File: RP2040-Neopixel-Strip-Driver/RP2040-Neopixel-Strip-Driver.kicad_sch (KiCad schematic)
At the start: 0 parts

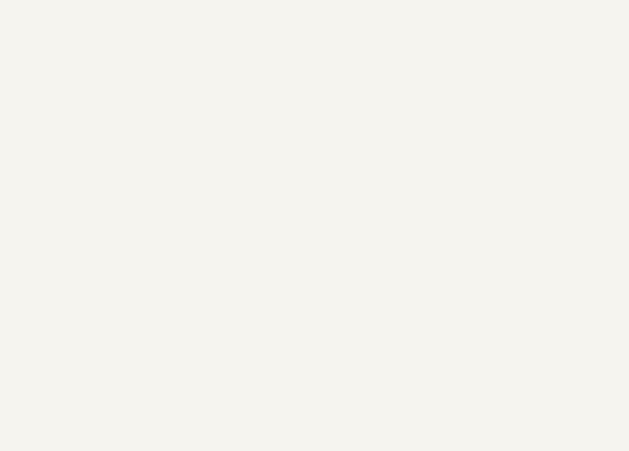
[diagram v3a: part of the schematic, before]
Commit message: Added level shifter
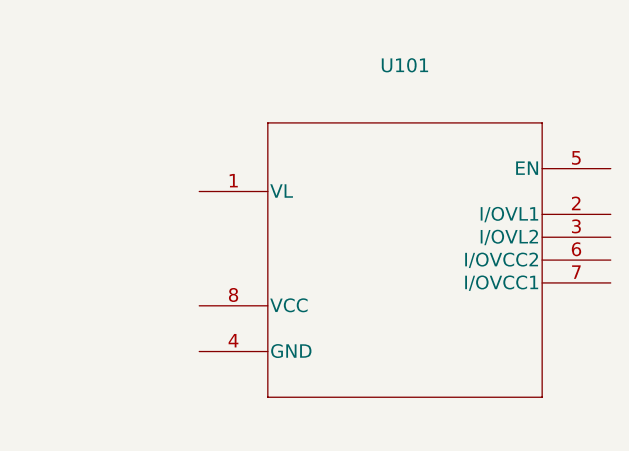
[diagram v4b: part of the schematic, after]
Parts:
- added U101: (no value), symbol NLSX4302EBMUTCG:NLSX4302EBMUTCG
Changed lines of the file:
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@@
     (comment 4 "https://github.com/mrangen/RP2040-Dev-Board")
+  )
+  (symbol (lib_id "NLSX4302EBMUTCG:NLSX4302EBMUTCG") (at 168.91 67.31 0) (unit 1)
+    (in_bom yes) (on_board yes) (fields_autoplaced)
+    (property "Reference" "U101" (id 0) (at 191.77 53.34 0)
+      (effects (font (size 1.524 1.524)))
+    )
+    (property "Value" "" (id 1) (at 191.77 57.15 0)
+      (effects (font (size 1.524 1.524)))
+    )
+    (property "Footprint" "" (id 2) (at 191.77 58.674 0)
+      (effects (font (size 1.524 1.524)) hide)
+    )
+    (property "Datasheet" "" (id 3) (at 168.91 67.31 0)
+      (effects (font (size 1.524 1.524)))
+    )
+    (property "JLCPCB P/N" "C893527" (id 4) (at 168.91 67.31 0)
+      (effects (font (size 1.27 1.27)) hide)
+    )
+    (pin "1")
+    (pin "2")
+    (pin "3")
+    (pin "4")
+    (pin "5")
+    (pin "6")
+    (pin "7")
+    (pin "8")
   )
   (sheet (at 82.55 50.8) (size 45.72 40.64) (fields_autoplaced)
@@
       (reference "SW202") (unit 1) (value "~{USB_BOOT}") (footprint "Breadstick Footprints:GT-TC029B-H025-L1N")
     )
+    (path "/61abfe14-530f-45cb-bac5-bff48de16e05"
+      (reference "U101") (unit 1) (value "NLSX4302EBMUTCG") (footprint "NLSX4302EBMUTCG:NLSX4302EBMUTCG")
+    )
     (path "/3e7bcc2a-10c2-45cd-9897-4c0007e1c7fc/00c3344e-81e0-498f-aca3-32f690281efd"

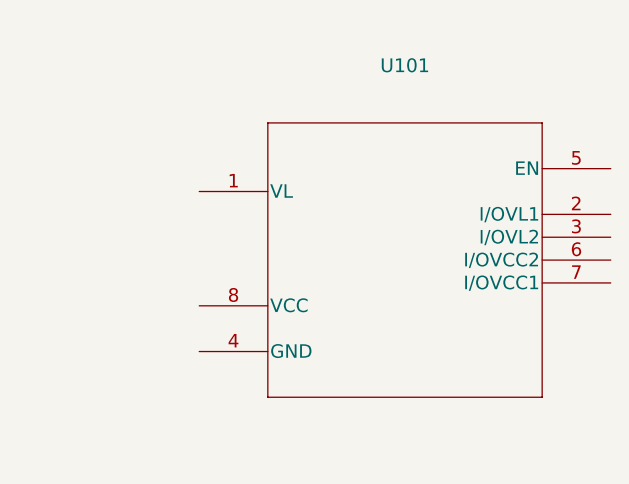
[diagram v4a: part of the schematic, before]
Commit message: Update RP2040-Neopixel-Strip-Driver.kicad_sch
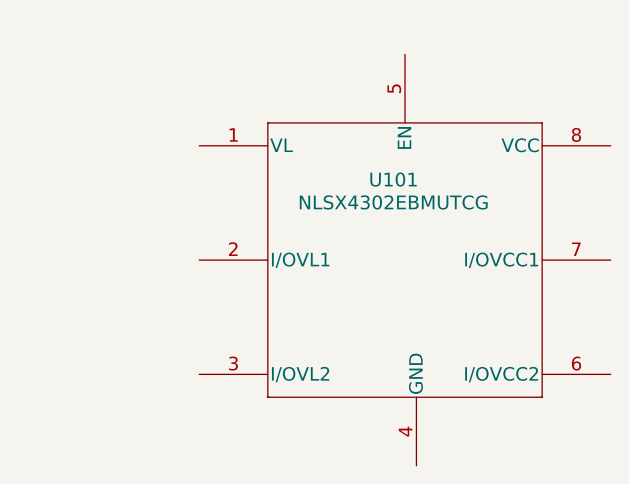
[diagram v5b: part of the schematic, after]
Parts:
- U101: value (none) -> NLSX4302EBMUTCG; footprint (none) -> NLSX4302EBMUTCG:NLSX4302EBMUTCG
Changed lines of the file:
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@@
   (symbol (lib_id "NLSX4302EBMUTCG:NLSX4302EBMUTCG") (at 168.91 67.31 0) (unit 1)
     (in_bom yes) (on_board yes) (fields_autoplaced)
-    (property "Reference" "U101" (id 0) (at 191.77 53.34 0)
+    (property "Reference" "U101" (id 0) (at 190.5 66.04 0)
       (effects (font (size 1.524 1.524)))
     )
-    (property "Value" "" (id 1) (at 191.77 57.15 0)
+    (property "Value" "NLSX4302EBMUTCG" (id 1) (at 190.5 68.58 0)
       (effects (font (size 1.524 1.524)))
     )
-    (property "Footprint" "" (id 2) (at 191.77 58.674 0)
+    (property "Footprint" "NLSX4302EBMUTCG:NLSX4302EBMUTCG" (id 2) (at 191.77 58.674 0)
       (effects (font (size 1.524 1.524)) hide)
     )

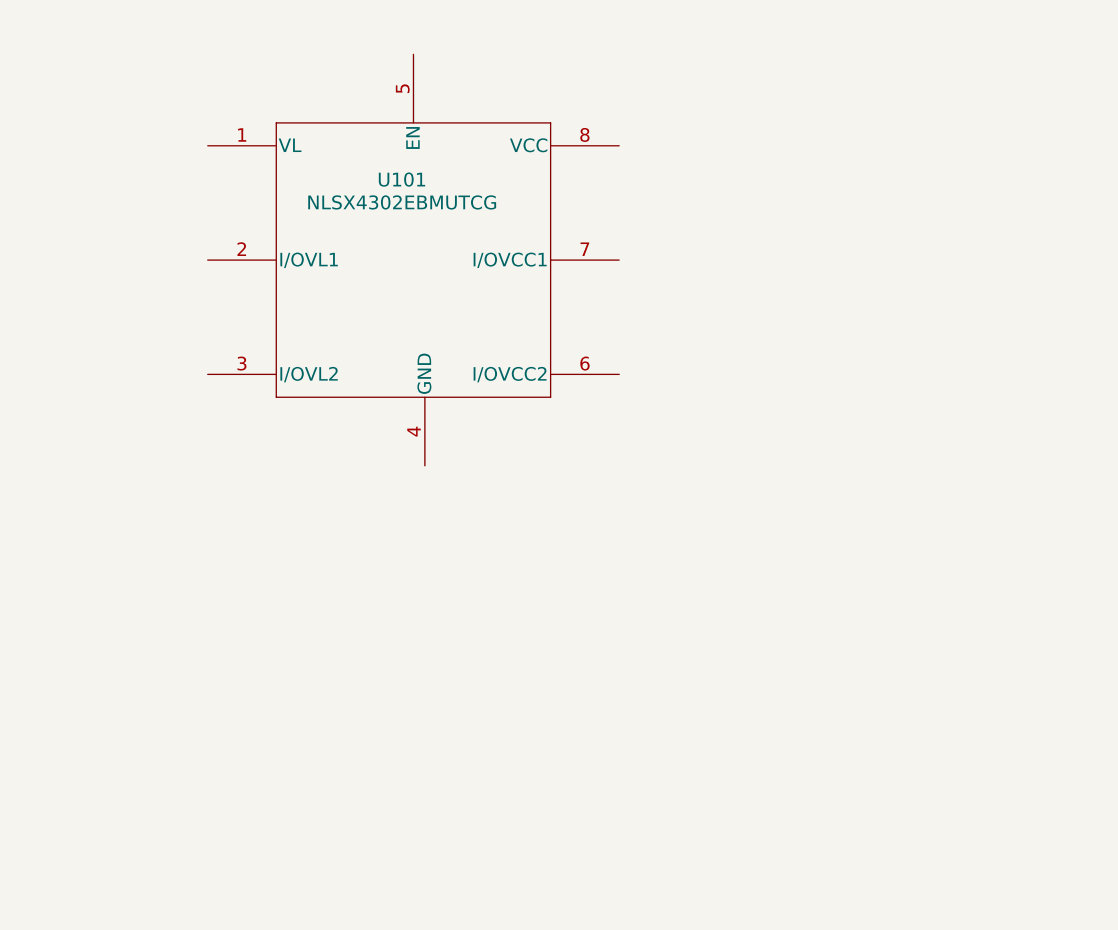
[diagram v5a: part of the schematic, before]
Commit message: Added model for level shifter and added 3Daccelerometer+3Dgyroscope
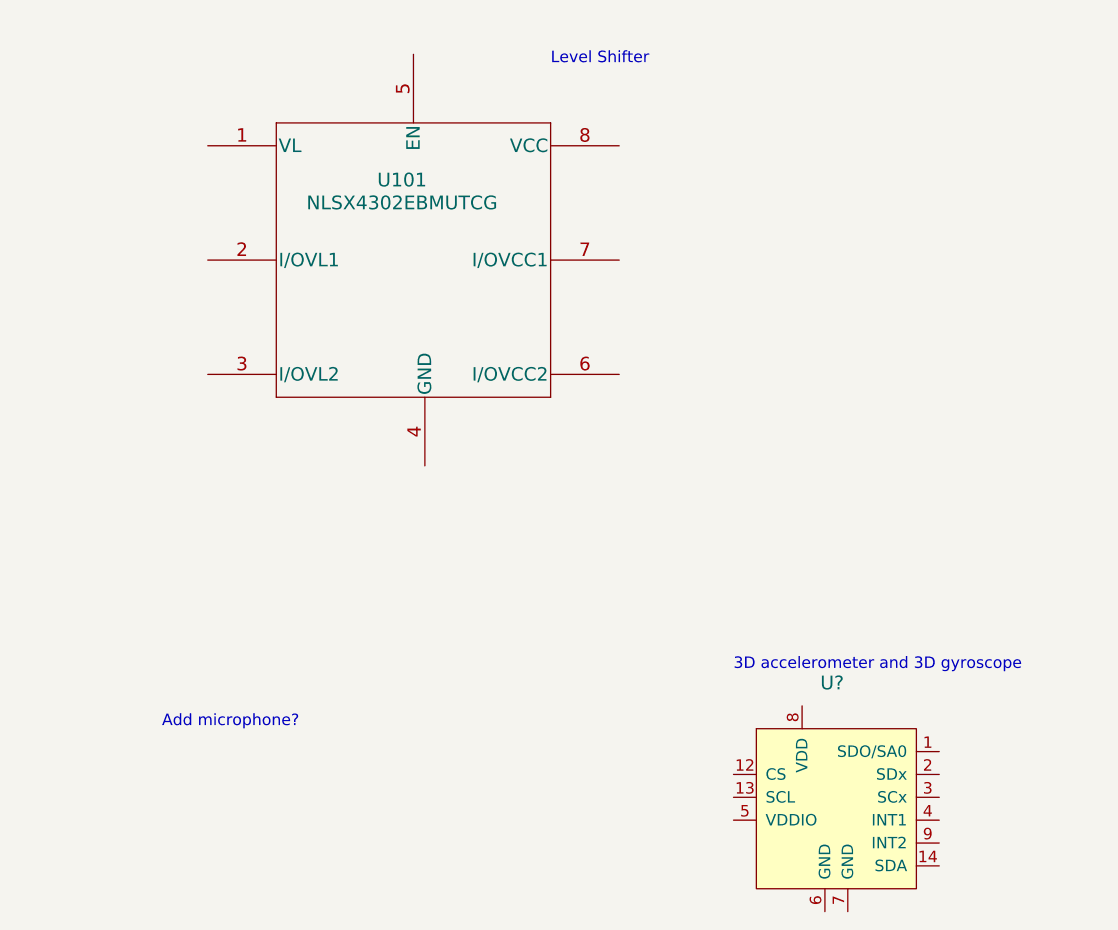
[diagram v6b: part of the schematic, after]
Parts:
- added U?: (no value), symbol dk_Motion-Sensors-IMUs-Inertial-Measurement-Units:LSM6DS3TR
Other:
- note added: "3D accelerometer and 3D gyroscope"
- note added: "Add microphone?"
- note added: "Level Shifter"
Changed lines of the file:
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@@
     (comment 4 "https://github.com/mrangen/RP2040-Dev-Board")
+  )
+  (text "Add microphone?" (at 163.83 127 0)
+    (effects (font (size 1.27 1.27)) (justify left bottom))
+  )
+  (text "Level Shifter\n" (at 207.01 53.34 0)
+    (effects (font (size 1.27 1.27)) (justify left bottom))
+  )
+  (text "3D accelerometer and 3D gyroscope" (at 227.33 120.65 0)
+    (effects (font (size 1.27 1.27)) (justify left bottom))
   )
   (symbol (lib_id "NLSX4302EBMUTCG:NLSX4302EBMUTCG") (at 168.91 67.31 0) (unit 1)
@@
     (pin "8")
   )
+  (symbol (lib_id "dk_Motion-Sensors-IMUs-Inertial-Measurement-Units:LSM6DS3TR") (at 237.49 137.16 0) (unit 1)
+    (in_bom yes) (on_board yes) (fields_autoplaced)
+    (property "Reference" "U?" (id 0) (at 236.9694 121.92 0)
+      (effects (font (size 1.524 1.524)) (justify left))
+    )
+    (property "Value" "" (id 1) (at 236.9694 125.73 0)
+      (effects (font (size 1.524 1.524)) (justify left))
+    )
+    (property "Footprint" "" (id 2) (at 242.57 132.08 0)
+      (effects (font (size 1.524 1.524)) (justify left) hide)
+    )
+    (property "Datasheet" "http://www.st.com/content/ccc/resource/technical/document/datasheet/a3/f5/4f/ae/8e/44/41/d7/DM00133076.pdf/files/DM00133076.pdf/jcr:content/translations/en.DM00133076.pdf" (id 3) (at 242.57 129.54 0)
+      (effects (font (size 1.524 1.524)) (justify left) hide)
+    )
+    (property "Digi-Key_PN" "497-15383-1-ND" (id 4) (at 242.57 127 0)
+      (effects (font (size 1.524 1.524)) (justify left) hide)
+    )
+    (property "MPN" "LSM6DS3TR" (id 5) (at 242.57 124.46 0)
+      (effects (font (size 1.524 1.524)) (justify left) hide)
+    )
+    (property "Category" "Sensors, Transducers" (id 6) (at 242.57 121.92 0)
+      (effects (font (size 1.524 1.524)) (justify left) hide)
+    )
+    (property "Family" "Motion Sensors - IMUs (Inertial Measurement Units)" (id 7) (at 242.57 119.38 0)
+      (effects (font (size 1.524 1.524)) (justify left) hide)
+    )
+    (property "DK_Datasheet_Link" "http://www.st.com/content/ccc/resource/technical/document/datasheet/a3/f5/4f/ae/8e/44/41/d7/DM00133076.pdf/files/DM00133076.pdf/jcr:content/translations/en.DM00133076.pdf" (id 8) (at 242.57 116.84 0)
+      (effects (font (size 1.524 1.524)) (justify left) hide)
+    )
+    (property "DK_Detail_Page" "/product-detail/en/stmicroelectronics/LSM6DS3TR/497-15383-1-ND/5180534" (id 9) (at 242.57 114.3 0)
+      (effects (font (size 1.524 1.524)) (justify left) hide)
+    )
+    (property "Description" "IMU ACCEL/GYRO I2C/SPI 14VFLGA" (id 10) (at 242.57 111.76 0)
+      (effects (font (size 1.524 1.524)) (justify left) hide)
+    )
+    (property "Manufacturer" "STMicroelectronics" (id 11) (at 242.57 109.22 0)
+      (effects (font (size 1.524 1.524)) (justify left) hide)
+    )
+    (property "Status" "Active" (id 12) (at 242.57 106.68 0)
+      (effects (font (size 1.524 1.524)) (justify left) hide)
+    )
+    (property "JLCPCB P/N" "C967633" (id 13) (at 237.49 137.16 0)
+      (effects (font (size 1.27 1.27)) hide)
+    )
+    (pin "1")
+    (pin "10")
+    (pin "11")
+    (pin "12")
+    (pin "13")
+    (pin "14")
+    (pin "2")
+    (pin "3")
+    (pin "4")
+    (pin "5")
+    (pin "6")
+    (pin "7")
+    (pin "8")
+    (pin "9")
+  )
   (sheet (at 82.55 50.8) (size 45.72 40.64) (fields_autoplaced)
     (stroke (width 0.1524) (type solid) (color 0 0 0 0))
@@
       (reference "U205") (unit 1) (value "W25Q128JVPIQ") (footprint "Package_SON:WSON-8-1EP_6x5mm_P1.27mm_EP3.4x4.3mm")
     )
+    (path "/e57cd689-f3bf-4a84-b820-dd33af7d6263"
+      (reference "U?") (unit 1) (value "LSM6DS3TR") (footprint "digikey-footprints:LGA-14L_2.5x3mm__LSM6DS3")
+    )
     (path "/3e7bcc2a-10c2-45cd-9897-4c0007e1c7fc/2a22be26-a817-4ed8-b112-95aa7d11fc7c"
